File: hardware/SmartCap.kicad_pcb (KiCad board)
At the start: 2 copper layers, 56.9 x 23.5 mm, 18 parts, among them J1 5034801000, J2 5034801000, J3 5034801000, J4 Conn_01x12_Female, J5 Conn_01x12_Female, Q1 Q_PNP_BCE, SW1 SW_Push, U1 ATtiny85-20SU

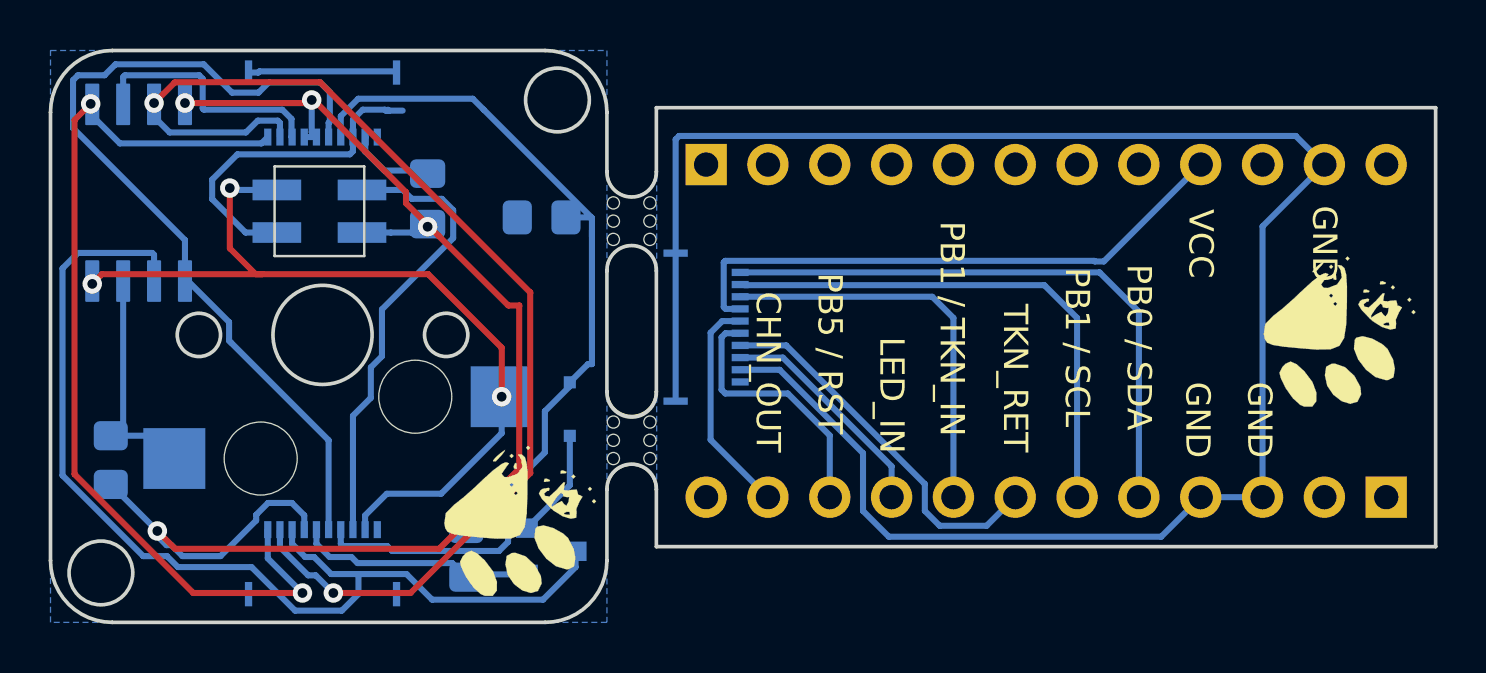
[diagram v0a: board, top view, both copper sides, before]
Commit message: Changing module to master mode for push updates instead of polling
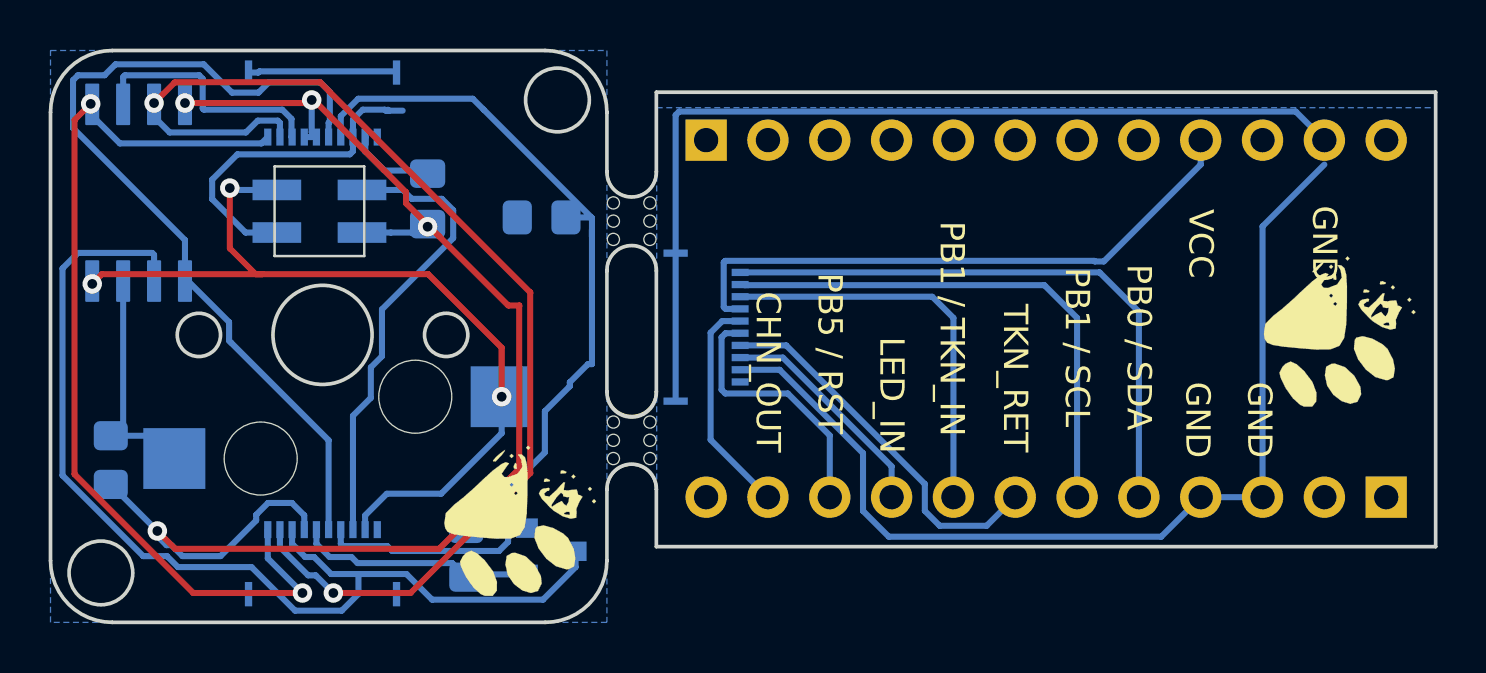
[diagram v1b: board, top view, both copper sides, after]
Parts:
- removed D1: DIODE, Diode_SMD:D_SOD-323F
- moved J5 1.00 mm to (167.9, 77.3)
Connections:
- Q1 pad 2: Net-(D1-Pad1) -> TOKEN_RET
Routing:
- net Net-(D1-Pad1): track 4.52 -> 0.00 mm
- net BREAKOUT_GND: track 79.0 -> 80.0 mm
- net BREAKOUT_VCC: track 23.8 -> 24.8 mm
- net TOKEN_RET: track 37.4 -> 38.1 mm
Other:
- outline, holes or cut-outs redrawn
